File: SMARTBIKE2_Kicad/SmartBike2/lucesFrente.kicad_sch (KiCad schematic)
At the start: 13 parts, among them Q5 SI2302, U3 LM358

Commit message: Revisión conjunta 29/10/23
Llamen a Dios
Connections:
- net Vswf: now also U3.3 (+); no longer U3.2 (-)
- net at RV1.2: now also U3.2 (-); no longer U3.3 (+)
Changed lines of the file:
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@@
   (junction (at 139.7 41.91) (diameter 0) (color 0 0 0 0)
   )
+  (junction (at 111.76 41.91) (diameter 0) (color 0 0 0 0)
+  )
   (junction (at 173.99 64.77) (diameter 0) (color 0 0 0 0)
-  )
-  (junction (at 111.76 41.91) (diameter 0) (color 0 0 0 0)
   )
   (junction (at 124.46 67.31) (diameter 0) (color 0 0 0 0)
@@
     (stroke (width 0) (type default))
   )
-  (wire (pts (xy 173.99 64.77) (xy 167.64 64.77))
-    (stroke (width 0) (type default))
-  )
   (wire (pts (xy 99.06 82.55) (xy 111.76 82.55))
     (stroke (width 0) (type default))
@@
     (stroke (width 0) (type default))
   )
+  (wire (pts (xy 167.64 64.77) (xy 173.99 64.77))
+    (stroke (width 0) (type default))
+  )
   (wire (pts (xy 105.41 151.13) (xy 105.41 162.56))
     (stroke (width 0) (type default))
@@
     (stroke (width 0) (type default))
   )
-  (wire (pts (xy 152.4 62.23) (xy 147.32 62.23))
-    (stroke (width 0) (type default))
-  )
   (wire (pts (xy 91.44 148.59) (xy 91.44 151.13))
     (stroke (width 0) (type default))
@@
     (stroke (width 0) (type default))
   )
+  (wire (pts (xy 147.32 62.23) (xy 152.4 62.23))
+    (stroke (width 0) (type default))
+  )
   (wire (pts (xy 80.01 41.91) (xy 99.06 41.91))
     (stroke (width 0) (type default))
@@
     (stroke (width 0) (type default))
   )
+  (wire (pts (xy 147.32 53.34) (xy 143.51 53.34))
+    (stroke (width 0) (type default))
+  )
+  (wire (pts (xy 124.46 69.85) (xy 124.46 67.31))
+    (stroke (width 0) (type default))
+  )
+  (wire (pts (xy 111.76 69.85) (xy 111.76 67.31))
+    (stroke (width 0) (type default))
+  )
+  (wire (pts (xy 99.06 38.1) (xy 99.06 41.91))
+    (stroke (width 0) (type default))
+  )
+  (wire (pts (xy 99.06 41.91) (xy 111.76 41.91))
+    (stroke (width 0) (type default))
+  )
+  (wire (pts (xy 80.01 82.55) (xy 99.06 82.55))
+    (stroke (width 0) (type default))
+  )
+  (wire (pts (xy 111.76 58.42) (xy 111.76 67.31))
+    (stroke (width 0) (type default))
+  )
   (wire (pts (xy 137.16 67.31) (xy 152.4 67.31))
-    (stroke (width 0) (type default))
-  )
-  (wire (pts (xy 147.32 53.34) (xy 143.51 53.34))
-    (stroke (width 0) (type default))
-  )
-  (wire (pts (xy 124.46 69.85) (xy 124.46 67.31))
-    (stroke (width 0) (type default))
-  )
-  (wire (pts (xy 111.76 69.85) (xy 111.76 67.31))
-    (stroke (width 0) (type default))
-  )
-  (wire (pts (xy 99.06 38.1) (xy 99.06 41.91))
-    (stroke (width 0) (type default))
-  )
-  (wire (pts (xy 99.06 41.91) (xy 111.76 41.91))
-    (stroke (width 0) (type default))
-  )
-  (wire (pts (xy 80.01 82.55) (xy 99.06 82.55))
-    (stroke (width 0) (type default))
-  )
-  (wire (pts (xy 111.76 58.42) (xy 111.76 67.31))
     (stroke (width 0) (type default))
   )
@@
     )
   )
-  (symbol (lib_id "Amplifier_Operational:LM358") (at 160.02 64.77 0) (unit 1)
-    (in_bom yes) (on_board yes) (dnp no) (fields_autoplaced)
-    (property "Reference" "U3" (at 160.02 54.61 0)
-      (effects (font (size 1.27 1.27)))
-    )
-    (property "Value" "LM358" (at 160.02 57.15 0)
-      (effects (font (size 1.27 1.27)))
-    )
+  (symbol (lib_id "Amplifier_Operational:LM358") (at 160.02 64.77 0) (mirror x) (unit 1)
+    (in_bom yes) (on_board yes) (dnp no)
+    (property "Reference" "U3" (at 160.02 74.93 0)
+      (effects (font (size 1.27 1.27)))
+    )
+    (property "Value" "LM358" (at 160.02 72.39 0)
+      (effects (font (size 1.27 1.27)))
+    )

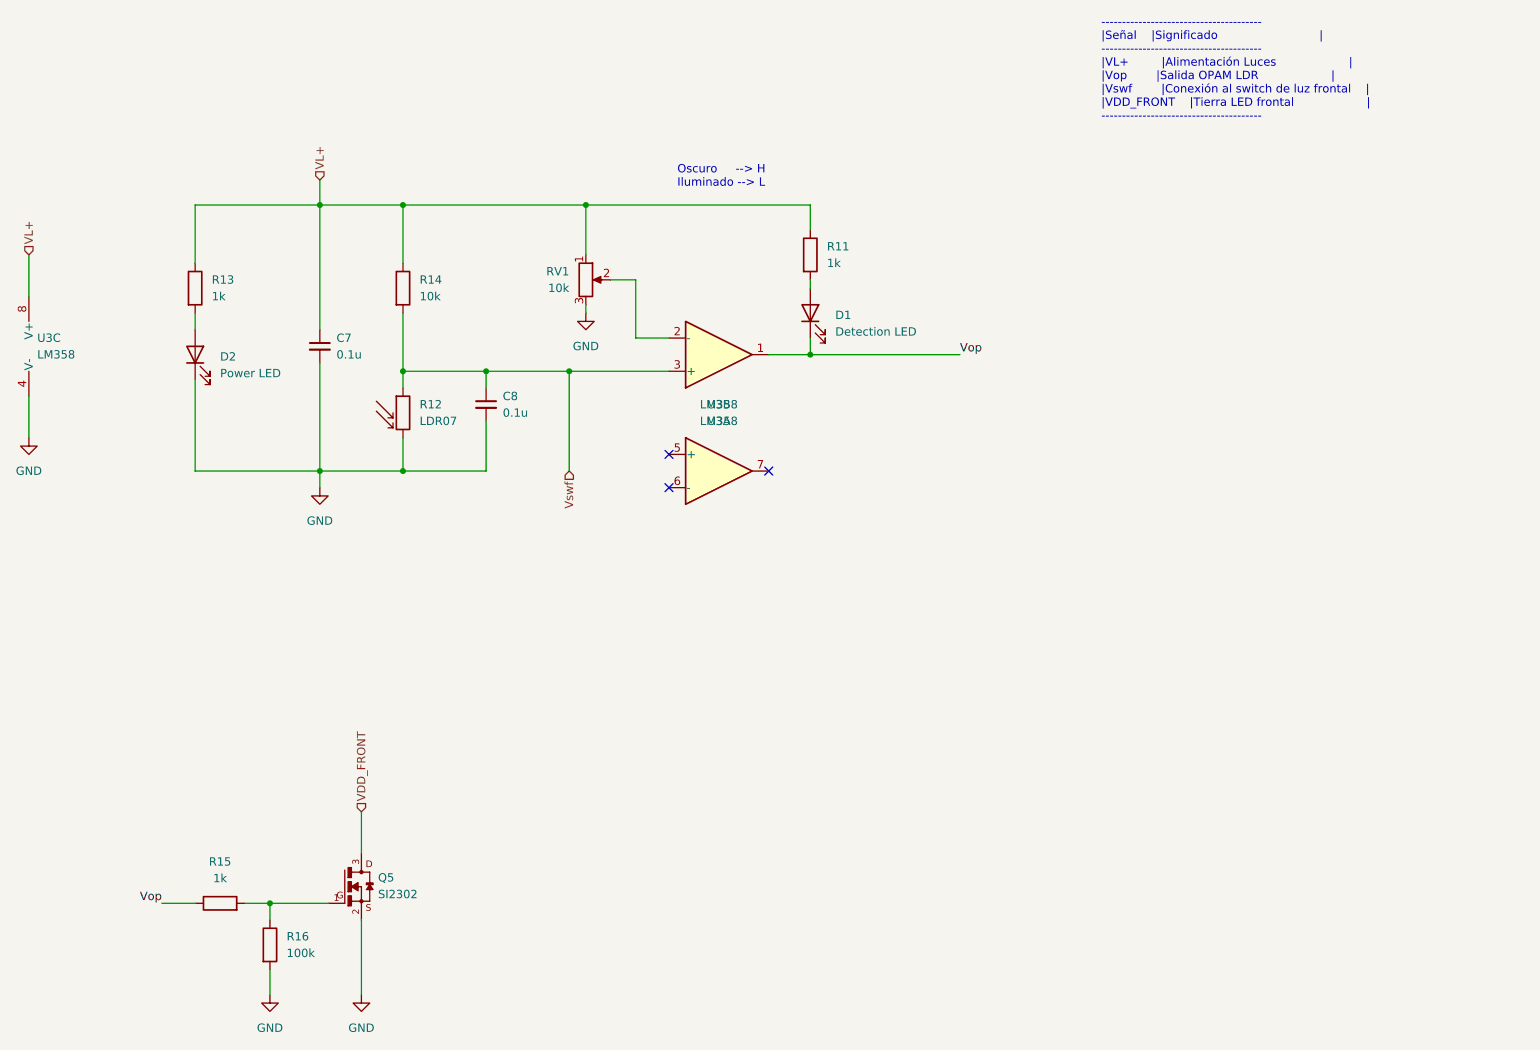
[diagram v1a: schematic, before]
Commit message: Beta 100% esquemáticos
+ Acondicionamiento ESP32

~ Huellas
~ PCB
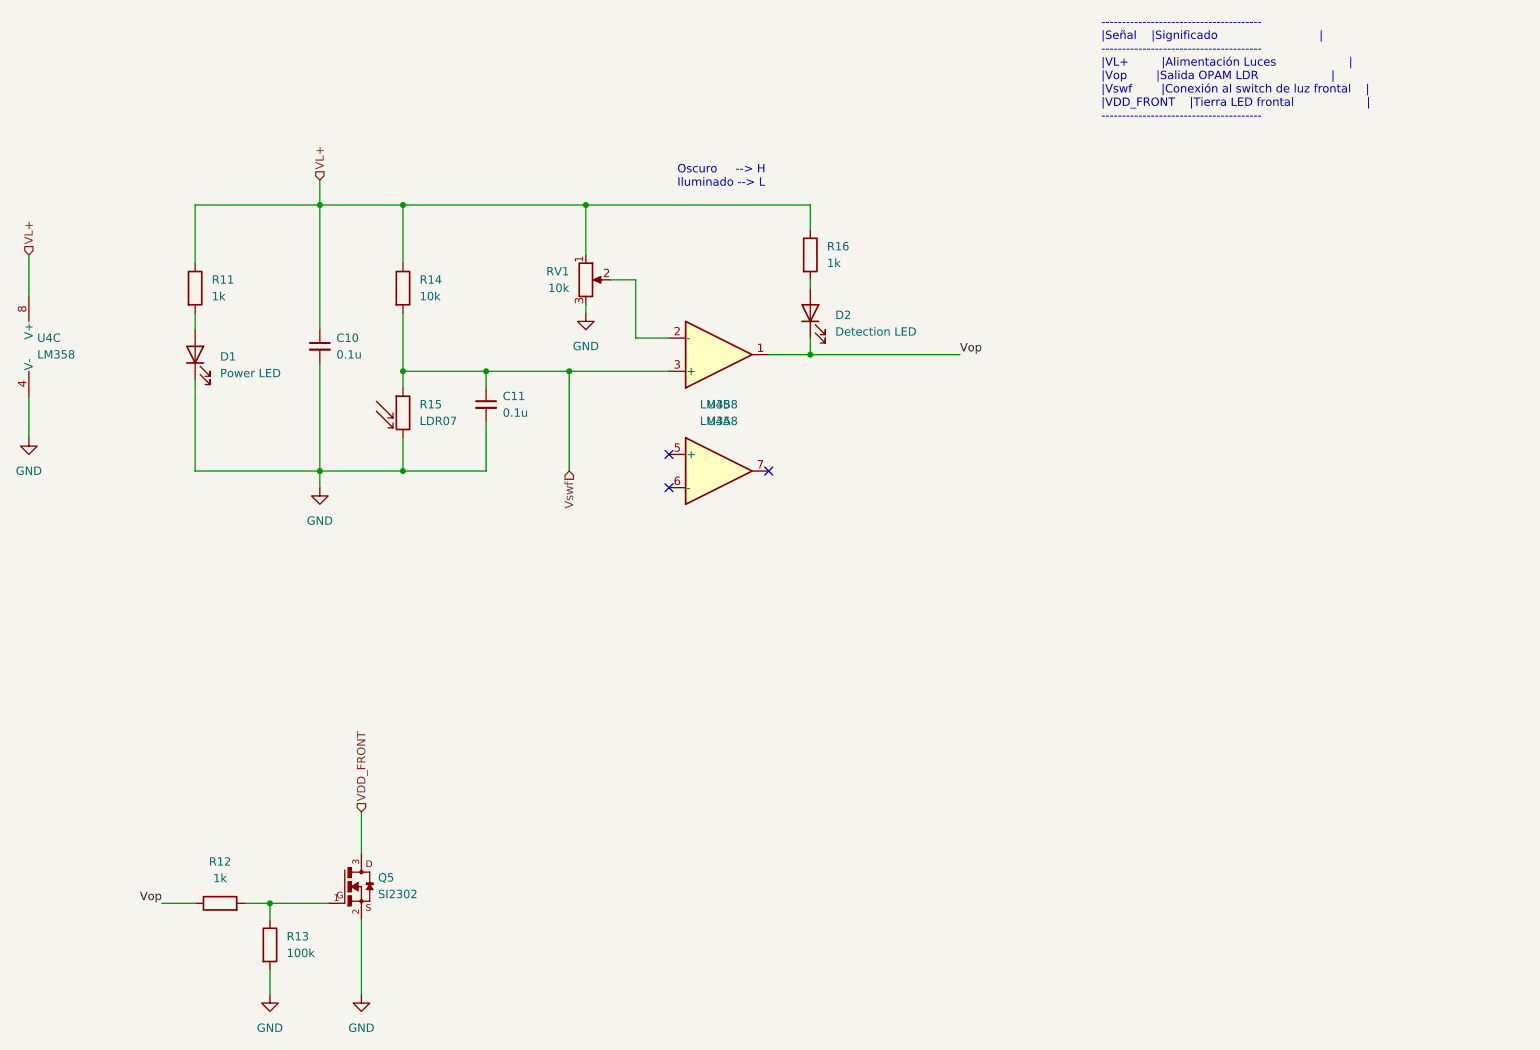
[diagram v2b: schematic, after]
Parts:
- renumbered C7 to C10, C8 to C11, D2 to D1, D1 to D2, R13 to R11, R15 to R12, R16 to R13, R12 to R15, R11 to R16, U3 to U4
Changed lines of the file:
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@@
   (symbol (lib_id "Device:R") (at 91.44 154.94 0) (unit 1)
     (in_bom yes) (on_board yes) (dnp no) (fields_autoplaced)
-    (property "Reference" "R16" (at 93.98 153.67 0)
+    (property "Reference" "R13" (at 93.98 153.67 0)
       (effects (font (size 1.27 1.27)) (justify left))
     )
@@
       (project "SmartBike2"
         (path "/ec60d9f0-678c-40dc-aaf4-e99b29a92238/524d1916-2b88-4ec8-8df8-acd48937d478/a50242bc-f2ef-4a73-9cd4-f9da3ac69681"
-          (reference "R16") (unit 1)
+          (reference "R13") (unit 1)
         )
       )
@@
   (symbol (lib_id "Amplifier_Operational:LM358") (at 57.15 63.5 0) (unit 3)
     (in_bom yes) (on_board yes) (dnp no) (fields_autoplaced)
-    (property "Reference" "U3" (at 55.88 62.23 0)
+    (property "Reference" "U4" (at 55.88 62.23 0)
       (effects (font (size 1.27 1.27)) (justify left))
     )
@@
       (project "SmartBike2"
         (path "/ec60d9f0-678c-40dc-aaf4-e99b29a92238/524d1916-2b88-4ec8-8df8-acd48937d478/a50242bc-f2ef-4a73-9cd4-f9da3ac69681"
-          (reference "U3") (unit 3)
+          (reference "U4") (unit 3)
         )
       )
@@
   (symbol (lib_id "Device:R") (at 80.01 54.61 0) (unit 1)
     (in_bom yes) (on_board yes) (dnp no) (fields_autoplaced)
-    (property "Reference" "R13" (at 82.55 53.34 0)
+    (property "Reference" "R11" (at 82.55 53.34 0)
       (effects (font (size 1.27 1.27)) (justify left))
     )
@@
       (project "SmartBike2"
         (path "/ec60d9f0-678c-40dc-aaf4-e99b29a92238/524d1916-2b88-4ec8-8df8-acd48937d478/a50242bc-f2ef-4a73-9cd4-f9da3ac69681"
-          (reference "R13") (unit 1)
+          (reference "R11") (unit 1)
         )
       )
@@
   (symbol (lib_id "Device:LED") (at 173.99 58.42 90) (unit 1)
     (in_bom yes) (on_board yes) (dnp no) (fields_autoplaced)
-    (property "Reference" "D1" (at 177.8 58.7375 90)
+    (property "Reference" "D2" (at 177.8 58.7375 90)
       (effects (font (size 1.27 1.27)) (justify right))
     )
@@
       (project "SmartBike2"
         (path "/ec60d9f0-678c-40dc-aaf4-e99b29a92238/524d1916-2b88-4ec8-8df8-acd48937d478/a50242bc-f2ef-4a73-9cd4-f9da3ac69681"
-          (reference "D1") (unit 1)
+          (reference "D2") (unit 1)
         )
       )
@@
   (symbol (lib_id "Device:R") (at 83.82 148.59 90) (unit 1)
     (in_bom yes) (on_board yes) (dnp no) (fields_autoplaced)
-    (property "Reference" "R15" (at 83.82 142.24 90)
+    (property "Reference" "R12" (at 83.82 142.24 90)
       (effects (font (size 1.27 1.27)))
     )
@@
       (project "SmartBike2"
         (path "/ec60d9f0-678c-40dc-aaf4-e99b29a92238/524d1916-2b88-4ec8-8df8-acd48937d478/a50242bc-f2ef-4a73-9cd4-f9da3ac69681"
-          (reference "R15") (unit 1)
+          (reference "R12") (unit 1)
         )
       )
@@
   (symbol (lib_id "power:GND") (at 91.44 162.56 0) (unit 1)
     (in_bom yes) (on_board yes) (dnp no) (fields_autoplaced)
-    (property "Reference" "#PWR017" (at 91.44 168.91 0)
+    (property "Reference" "#PWR022" (at 91.44 168.91 0)
       (effects (font (size 1.27 1.27)) hide)
     )
@@
       (project "SmartBike2"
         (path "/ec60d9f0-678c-40dc-aaf4-e99b29a92238/524d1916-2b88-4ec8-8df8-acd48937d478/a50242bc-f2ef-4a73-9cd4-f9da3ac69681"
-          (reference "#PWR017") (unit 1)
+          (reference "#PWR022") (unit 1)
         )
       )
@@
   (symbol (lib_id "power:GND") (at 99.06 85.09 0) (unit 1)
     (in_bom yes) (on_board yes) (dnp no) (fields_autoplaced)
-    (property "Reference" "#PWR014" (at 99.06 91.44 0)
+    (property "Reference" "#PWR023" (at 99.06 91.44 0)
       (effects (font (size 1.27 1.27)) hide)
     )
@@
       (project "SmartBike2"
         (path "/ec60d9f0-678c-40dc-aaf4-e99b29a92238/524d1916-2b88-4ec8-8df8-acd48937d478/a50242bc-f2ef-4a73-9cd4-f9da3ac69681"
-          (reference "#PWR014") (unit 1)
+          (reference "#PWR023") (unit 1)
         )
       )
@@
   (symbol (lib_id "power:GND") (at 54.61 77.47 0) (unit 1)
     (in_bom yes) (on_board yes) (dnp no) (fields_autoplaced)
-    (property "Reference" "#PWR015" (at 54.61 83.82 0)
+    (property "Reference" "#PWR021" (at 54.61 83.82 0)
       (effects (font (size 1.27 1.27)) hide)
     )
@@
       (project "SmartBike2"
         (path "/ec60d9f0-678c-40dc-aaf4-e99b29a92238/524d1916-2b88-4ec8-8df8-acd48937d478/a50242bc-f2ef-4a73-9cd4-f9da3ac69681"
-          (reference "#PWR015") (unit 1)
+          (reference "#PWR021") (unit 1)
         )
       )
@@
   (symbol (lib_id "Device:R") (at 173.99 49.53 0) (unit 1)
     (in_bom yes) (on_board yes) (dnp no) (fields_autoplaced)
-    (property "Reference" "R11" (at 176.53 48.26 0)
+    (property "Reference" "R16" (at 176.53 48.26 0)
       (effects (font (size 1.27 1.27)) (justify left))
     )
@@
       (project "SmartBike2"
         (path "/ec60d9f0-678c-40dc-aaf4-e99b29a92238/524d1916-2b88-4ec8-8df8-acd48937d478/a50242bc-f2ef-4a73-9cd4-f9da3ac69681"
-          (reference "R11") (unit 1)
+          (reference "R16") (unit 1)
         )
       )
@@
   (symbol (lib_id "Amplifier_Operational:LM358") (at 160.02 64.77 0) (mirror x) (unit 1)
     (in_bom yes) (on_board yes) (dnp no)
-    (property "Reference" "U3" (at 160.02 74.93 0)
+    (property "Reference" "U4" (at 160.02 74.93 0)
       (effects (font (size 1.27 1.27)))
     )
@@
       (project "SmartBike2"
         (path "/ec60d9f0-678c-40dc-aaf4-e99b29a92238/524d1916-2b88-4ec8-8df8-acd48937d478/a50242bc-f2ef-4a73-9cd4-f9da3ac69681"
-          (reference "U3") (unit 1)
+          (reference "U4") (unit 1)
         )
       )
@@
   (symbol (lib_id "Device:C_Small") (at 124.46 72.39 0) (unit 1)
     (in_bom yes) (on_board yes) (dnp no) (fields_autoplaced)
-    (property "Reference" "C8" (at 127 71.1263 0)
+    (property "Reference" "C11" (at 127 71.1263 0)
       (effects (font (size 1.27 1.27)) (justify left))
     )
@@
       (project "SmartBike2"
         (path "/ec60d9f0-678c-40dc-aaf4-e99b29a92238/524d1916-2b88-4ec8-8df8-acd48937d478/a50242bc-f2ef-4a73-9cd4-f9da3ac69681"
-          (reference "C8") (unit 1)
+          (reference "C11") (unit 1)
         )
       )
@@
   (symbol (lib_id "Sensor_Optical:LDR07") (at 111.76 73.66 0) (unit 1)
     (in_bom yes) (on_board yes) (dnp no) (fields_autoplaced)
-    (property "Reference" "R12" (at 114.3 72.39 0)
+    (property "Reference" "R15" (at 114.3 72.39 0)
       (effects (font (size 1.27 1.27)) (justify left))
     )
@@
       (project "SmartBike2"
         (path "/ec60d9f0-678c-40dc-aaf4-e99b29a92238/524d1916-2b88-4ec8-8df8-acd48937d478/a50242bc-f2ef-4a73-9cd4-f9da3ac69681"
-          (reference "R12") (unit 1)
+          (reference "R15") (unit 1)
         )
       )
@@
   (symbol (lib_id "power:GND") (at 105.41 162.56 0) (unit 1)
     (in_bom yes) (on_board yes) (dnp no) (fields_autoplaced)
-    (property "Reference" "#PWR016" (at 105.41 168.91 0)
+    (property "Reference" "#PWR024" (at 105.41 168.91 0)
       (effects (font (size 1.27 1.27)) hide)
     )
@@
       (project "SmartBike2"
         (path "/ec60d9f0-678c-40dc-aaf4-e99b29a92238/524d1916-2b88-4ec8-8df8-acd48937d478/a50242bc-f2ef-4a73-9cd4-f9da3ac69681"
-          (reference "#PWR016") (unit 1)
+          (reference "#PWR024") (unit 1)
         )
       )
@@
   (symbol (lib_id "Amplifier_Operational:LM358") (at 160.02 82.55 0) (unit 2)
     (in_bom yes) (on_board yes) (dnp no) (fields_autoplaced)
-    (property "Reference" "U3" (at 160.02 72.39 0)
+    (property "Reference" "U4" (at 160.02 72.39 0)
       (effects (font (size 1.27 1.27)))
     )
@@
       (project "SmartBike2"
         (path "/ec60d9f0-678c-40dc-aaf4-e99b29a92238/524d1916-2b88-4ec8-8df8-acd48937d478/a50242bc-f2ef-4a73-9cd4-f9da3ac69681"
-          (reference "U3") (unit 2)
+          (reference "U4") (unit 2)
         )
       )
@@
   (symbol (lib_id "Device:C_Small") (at 99.06 63.5 0) (unit 1)
     (in_bom yes) (on_board yes) (dnp no) (fields_autoplaced)
-    (property "Reference" "C7" (at 101.6 62.2363 0)
+    (property "Reference" "C10" (at 101.6 62.2363 0)
       (effects (font (size 1.27 1.27)) (justify left))
     )
@@
       (project "SmartBike2"
         (path "/ec60d9f0-678c-40dc-aaf4-e99b29a92238/524d1916-2b88-4ec8-8df8-acd48937d478/a50242bc-f2ef-4a73-9cd4-f9da3ac69681"
-          (reference "C7") (unit 1)
+          (reference "C10") (unit 1)
         )
       )
@@
   (symbol (lib_id "power:GND") (at 139.7 58.42 0) (unit 1)
     (in_bom yes) (on_board yes) (dnp no) (fields_autoplaced)
-    (property "Reference" "#PWR013" (at 139.7 64.77 0)
+    (property "Reference" "#PWR025" (at 139.7 64.77 0)
       (effects (font (size 1.27 1.27)) hide)
     )
@@
       (project "SmartBike2"
         (path "/ec60d9f0-678c-40dc-aaf4-e99b29a92238/524d1916-2b88-4ec8-8df8-acd48937d478/a50242bc-f2ef-4a73-9cd4-f9da3ac69681"
-          (reference "#PWR013") (unit 1)
+          (reference "#PWR025") (unit 1)
         )
       )
@@
   (symbol (lib_id "Device:LED") (at 80.01 64.77 90) (unit 1)
     (in_bom yes) (on_board yes) (dnp no) (fields_autoplaced)
-    (property "Reference" "D2" (at 83.82 65.0875 90)
+    (property "Reference" "D1" (at 83.82 65.0875 90)
       (effects (font (size 1.27 1.27)) (justify right))
     )
@@
       (project "SmartBike2"
         (path "/ec60d9f0-678c-40dc-aaf4-e99b29a92238/524d1916-2b88-4ec8-8df8-acd48937d478/a50242bc-f2ef-4a73-9cd4-f9da3ac69681"
-          (reference "D2") (unit 1)
-        )
-      )
+          (reference "D1") (unit 1)
+        )
+      )

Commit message: cache
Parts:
- C10, C11: footprint (none) -> Capacitor_SMD:C_0805_2012Metric_Pad1.18x1.45mm_HandSolder
- D1, D2: footprint (none) -> LED_SMD:LED_1206_3216Metric_Pad1.42x1.75mm_HandSolder
- Q5: footprint SI2302:SOT23 -> Package_TO_SOT_SMD:SOT-23
- U4: footprint (none) -> Package_SO:SO-8_3.9x4.9mm_P1.27mm
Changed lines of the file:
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@@
       (effects (font (size 1.27 1.27)) (justify left))
     )
-    (property "Footprint" "" (at 57.15 63.5 0)
+    (property "Footprint" "Package_SO:SO-8_3.9x4.9mm_P1.27mm" (at 57.15 63.5 0)
       (effects (font (size 1.27 1.27)) hide)
     )
@@
       (effects (font (size 1.27 1.27)) (justify right))
     )
-    (property "Footprint" "" (at 173.99 58.42 0)
+    (property "Footprint" "LED_SMD:LED_1206_3216Metric_Pad1.42x1.75mm_HandSolder" (at 173.99 58.42 0)
       (effects (font (size 1.27 1.27)) hide)
     )
@@
       (effects (font (size 1.27 1.27)) (justify left))
     )
-    (property "Footprint" "SI2302:SOT23" (at 105.41 146.05 0)
+    (property "Footprint" "Package_TO_SOT_SMD:SOT-23" (at 105.41 146.05 0)
       (effects (font (size 1.27 1.27)) (justify bottom) hide)
     )
@@
       (effects (font (size 1.27 1.27)))
     )
-    (property "Footprint" "" (at 160.02 64.77 0)
+    (property "Footprint" "Package_SO:SO-8_3.9x4.9mm_P1.27mm" (at 160.02 64.77 0)
       (effects (font (size 1.27 1.27)) hide)
     )
@@
       (effects (font (size 1.27 1.27)) (justify left))
     )
-    (property "Footprint" "" (at 124.46 72.39 0)
+    (property "Footprint" "Capacitor_SMD:C_0805_2012Metric_Pad1.18x1.45mm_HandSolder" (at 124.46 72.39 0)
       (effects (font (size 1.27 1.27)) hide)
     )
@@
       (effects (font (size 1.27 1.27)))
     )
-    (property "Footprint" "" (at 160.02 82.55 0)
+    (property "Footprint" "Package_SO:SO-8_3.9x4.9mm_P1.27mm" (at 160.02 82.55 0)
       (effects (font (size 1.27 1.27)) hide)
     )
@@
       (effects (font (size 1.27 1.27)) (justify left))
     )
-    (property "Footprint" "" (at 99.06 63.5 0)
+    (property "Footprint" "Capacitor_SMD:C_0805_2012Metric_Pad1.18x1.45mm_HandSolder" (at 99.06 63.5 0)
       (effects (font (size 1.27 1.27)) hide)
     )
@@
       (effects (font (size 1.27 1.27)) (justify right))
     )
-    (property "Footprint" "" (at 80.01 64.77 0)
-      (effects (font (size 1.27 1.27)) hide)
-    )
+    (property "Footprint" "LED_SMD:LED_1206_3216Metric_Pad1.42x1.75mm_HandSolder" (at 80.01 64.77 0)
+      (effects (font (size 1.27 1.27)) hide)
+    )
